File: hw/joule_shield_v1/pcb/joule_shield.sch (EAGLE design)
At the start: 136 parts, among them J1 MF-CON-MICROUSB-RIGHT, J4 USB_AUSB_A_SMT_RA, J5 JST-ZH5JST_ZH_SMT_VERT, J6 INTEL_JOULE_J6, J7 INTEL_JOULE_J7, SW1 MF-SW-TACT-4.2MM, SW2 MF-SW-TACT-4.2MM, SW3 MF-SW-TACT-4.2MM, U1 BQ25892PWQFN-24, U10 FT231XQFN-20, U11 MF-DSC-SOT233-MMBT3904, U12 MF-DSC-SOT233-MMBT3904, U13 MF-DSC-SOT233-MMBT3904, U14 MF-DSC-SOT233-MMBT3904, U2 FAN8623WLCSP16, U3 TPS63201PVSON-14, U4 TLV62084PWSON-8, U5 TPS2553PWSON-6, U6 TPS2553PWSON-6, U7 SINGLE-BIT_BUS_TRANSCEIVER, U8 SINGLE-BIT_BUS_TRANSCEIVER, U9 TXS0206-29

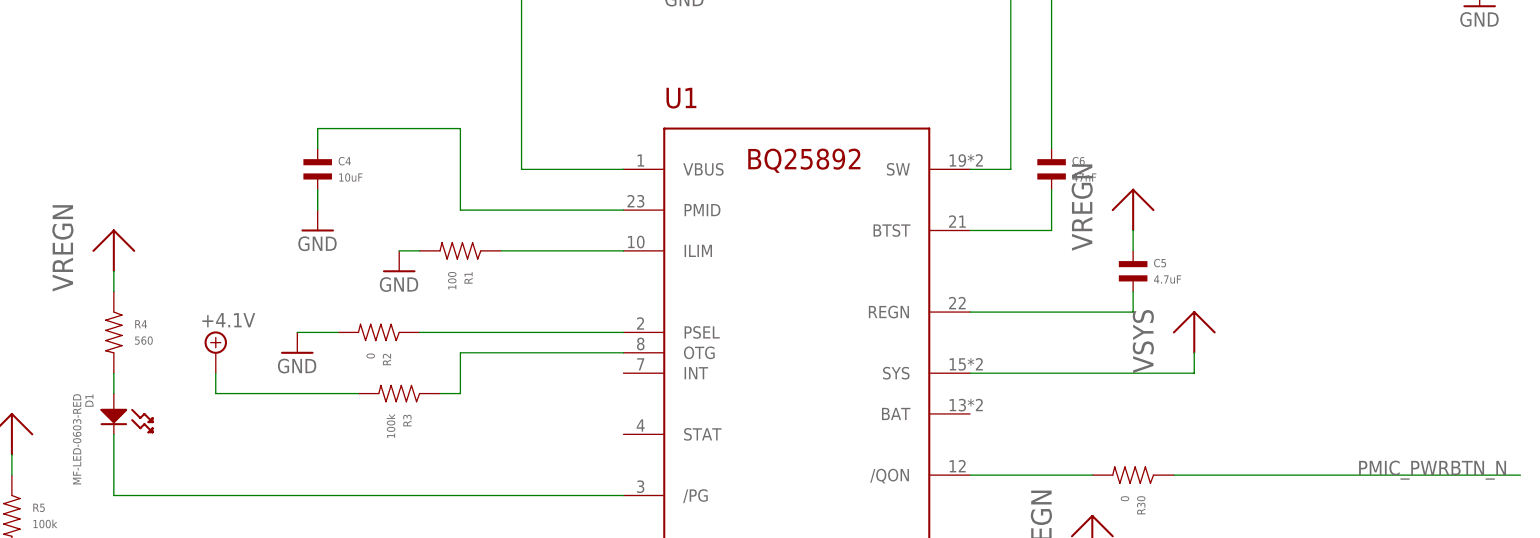
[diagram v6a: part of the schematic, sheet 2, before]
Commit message: joule shield: continue work on draft placement
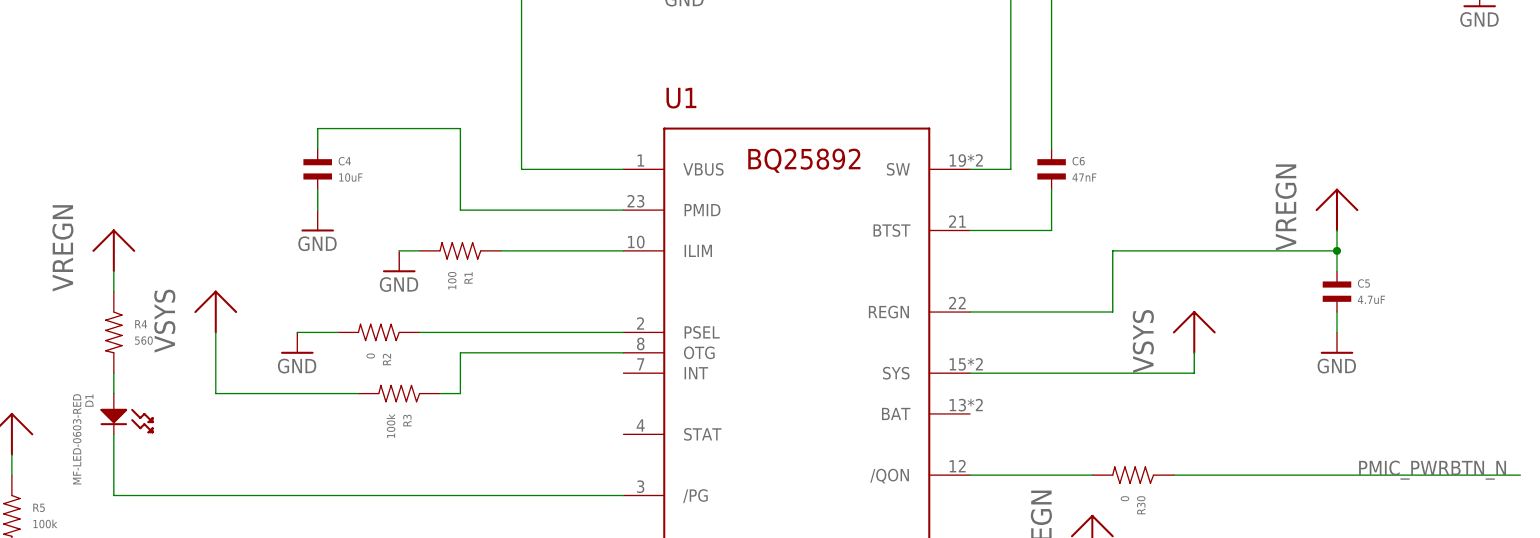
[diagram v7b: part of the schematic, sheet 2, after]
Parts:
- renumbered U$40 to J8
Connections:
- removed net +4.1V: R3.P$2
- removed net N$10: C5.P$2, U1.REGN
- net GND: now also C5.P$2
- net VREGN: now also U1.REGN
- net VSYS: now also R3.P$2
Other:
- moved on the sheet: C5
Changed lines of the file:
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@@
 <attribute name="MPN" value="MF-RES-0603-100K"/>
 </part>
-<part name="SUPPLY1" library="supply2" deviceset="+4.1V" device=""/>
 <part name="D1" library="mf_leds" deviceset="LED_SINGLE" device="-0603-RED" value="MF-LED-0603-RED"/>
 <part name="R4" library="mf_passives" deviceset="RESISTOR" device="_0603" value="560">
@@
 <part name="GND38" library="supply1" deviceset="GND" device=""/>
 <part name="GND39" library="supply1" deviceset="GND" device=""/>
-<part name="U$40" library="joule_shield" deviceset="DM3AT" device="DM3AT"/>
+<part name="J8" library="joule_shield" deviceset="DM3AT" device="DM3AT"/>
 <part name="GND40" library="supply1" deviceset="GND" device=""/>
 <part name="C36" library="mf_passives" deviceset="CAPACITOR_NP" device="_0603" value="0.1uF">
@@
 <part name="U$54" library="joule_shield" deviceset="M2.5MOUNT" device=""/>
 <part name="U$55" library="joule_shield" deviceset="M2.5MOUNT" device=""/>
+<part name="GND52" library="supply1" deviceset="GND" device=""/>
+<part name="U$40" library="joule_shield" deviceset="VSYS" device=""/>
 </parts>
 <sheets>
@@
 <instance part="GND4" gate="1" x="33.02" y="40.64"/>
 <instance part="R3" gate="G$1" x="45.72" y="35.56" rot="R270"/>
-<instance part="SUPPLY1" gate="P" x="22.86" y="40.64"/>
 <instance part="D1" gate="G$1" x="10.16" y="33.02" rot="R270"/>
 <instance part="R4" gate="G$1" x="10.16" y="43.18"/>
@@
 <instance part="R7" gate="G$1" x="132.08" y="-5.08"/>
 <instance part="GND6" gate="1" x="132.08" y="-15.24"/>
-<instance part="C5" gate="G$1" x="137.16" y="50.8">
-<attribute name="DPN" x="137.16" y="50.8" size="1.778" layer="96" display="off"/>
+<instance part="C5" gate="G$1" x="162.56" y="48.26">
+<attribute name="DPN" x="162.56" y="48.26" size="1.778" layer="96" display="off"/>
 </instance>
 <instance part="C6" gate="G$1" x="127" y="63.5">
@@
 <instance part="U$15" gate="G$1" x="180.34" y="99.06"/>
 <instance part="U$16" gate="G$1" x="144.78" y="40.64"/>
-<instance part="U$17" gate="G$1" x="137.16" y="55.88"/>
+<instance part="U$17" gate="G$1" x="162.56" y="55.88"/>
 <instance part="U$18" gate="G$1" x="132.08" y="15.24"/>
 <instance part="U$19" gate="G$1" x="10.16" y="50.8"/>
 <instance part="U$20" gate="G$1" x="60.96" y="109.22"/>
 <instance part="R30" gate="G$1" x="137.16" y="25.4" rot="R270"/>
+<instance part="GND52" gate="1" x="162.56" y="40.64"/>
+<instance part="U$40" gate="G$1" x="22.86" y="43.18"/>
 </instances>
 <busses>
@@
 <junction x="180.34" y="86.36"/>
 </segment>
+<segment>
+<pinref part="C5" gate="G$1" pin="P$2"/>
+<pinref part="GND52" gate="1" pin="GND"/>
+<wire x1="162.56" y1="45.72" x2="162.56" y2="43.18" width="0.1524" layer="91"/>
+</segment>
 </net>
 <net name="N$2" class="0">
@@
 <pinref part="U1" gate="G$1" pin="PSEL"/>
 <wire x1="48.26" y1="43.18" x2="73.66" y2="43.18" width="0.1524" layer="91"/>
-</segment>
-</net>
-<net name="+4.1V" class="0">
-<segment>
-<pinref part="SUPPLY1" gate="P" pin="+4.1V"/>
-<wire x1="22.86" y1="38.1" x2="22.86" y2="35.56" width="0.1524" layer="91"/>
-<pinref part="R3" gate="G$1" pin="P$2"/>
-<wire x1="22.86" y1="35.56" x2="40.64" y2="35.56" width="0.1524" layer="91"/>
 </segment>
 </net>
@@
 <pinref part="U1" gate="G$1" pin="TS"/>
 <wire x1="119.38" y1="10.16" x2="116.84" y2="10.16" width="0.1524" layer="91"/>
-</segment>
-</net>
-<net name="N$10" class="0">
-<segment>
-<pinref part="C5" gate="G$1" pin="P$2"/>
-<wire x1="137.16" y1="48.26" x2="137.16" y2="45.72" width="0.1524" layer="91"/>
-<pinref part="U1" gate="G$1" pin="REGN"/>
-<wire x1="137.16" y1="45.72" x2="116.84" y2="45.72" width="0.1524" layer="91"/>
 </segment>
 </net>
@@
 <pinref part="U$16" gate="G$1" pin="VSYS"/>
 </segment>
+<segment>
+<pinref part="R3" gate="G$1" pin="P$2"/>
+<wire x1="22.86" y1="35.56" x2="40.64" y2="35.56" width="0.1524" layer="91"/>
+<pinref part="U$40" gate="G$1" pin="VSYS"/>
+<wire x1="22.86" y1="35.56" x2="22.86" y2="43.18" width="0.1524" layer="91"/>
+</segment>
 </net>
 <net name="VREGN" class="0">
-<segment>
-<pinref part="C5" gate="G$1" pin="P$1"/>
-<wire x1="137.16" y1="53.34" x2="137.16" y2="55.88" width="0.1524" layer="91"/>
-<pinref part="U$17" gate="G$1" pin="VREGN"/>
-</segment>
 <segment>
 <pinref part="R6" gate="G$1" pin="P$1"/>
@@
 <wire x1="10.16" y1="50.8" x2="10.16" y2="48.26" width="0.1524" layer="91"/>
 <pinref part="U$19" gate="G$1" pin="VREGN"/>
+</segment>
+<segment>
+<pinref part="U1" gate="G$1" pin="REGN"/>
+<wire x1="116.84" y1="45.72" x2="134.62" y2="45.72" width="0.1524" layer="91"/>
+<wire x1="134.62" y1="45.72" x2="134.62" y2="53.34" width="0.1524" layer="91"/>
+<wire x1="134.62" y1="53.34" x2="162.56" y2="53.34" width="0.1524" layer="91"/>
+<pinref part="U$17" gate="G$1" pin="VREGN"/>
+<wire x1="162.56" y1="53.34" x2="162.56" y2="55.88" width="0.1524" layer="91"/>
+<pinref part="C5" gate="G$1" pin="P$1"/>
+<wire x1="162.56" y1="53.34" x2="162.56" y2="50.8" width="0.1524" layer="91"/>
+<junction x="162.56" y="53.34"/>
 </segment>
 </net>
@@
 <instance part="GND38" gate="1" x="-15.24" y="-10.16"/>
 <instance part="GND39" gate="1" x="40.64" y="22.86"/>
-<instance part="U$40" gate="G$1" x="177.8" y="22.86" rot="R180"/>
+<instance part="J8" gate="G$1" x="177.8" y="22.86" rot="R180"/>
 <instance part="GND40" gate="1" x="147.32" y="2.54"/>
 <instance part="C36" gate="G$1" x="147.32" y="58.42"/>
@@
 <pinref part="U9" gate="G$1" pin="VCCB"/>
 <wire x1="127" y1="66.04" x2="81.28" y2="66.04" width="0.1524" layer="91"/>
-<pinref part="U$40" gate="G$1" pin="VDD"/>
+<pinref part="J8" gate="G$1" pin="VDD"/>
 <wire x1="162.56" y1="30.48" x2="127" y2="30.48" width="0.1524" layer="91"/>
 <wire x1="127" y1="30.48" x2="127" y2="66.04" width="0.1524" layer="91"/>
@@
 </segment>
 <segment>
-<pinref part="U$40" gate="G$1" pin="GND"/>
+<pinref part="J8" gate="G$1" pin="GND"/>
 <wire x1="162.56" y1="33.02" x2="147.32" y2="33.02" width="0.1524" layer="91"/>
 <pinref part="GND40" gate="1" pin="GND"/>
 <wire x1="147.32" y1="33.02" x2="147.32" y2="27.94" width="0.1524" layer="91"/>
-<pinref part="U$40" gate="G$1" pin="VSS"/>
+<pinref part="J8" gate="G$1" pin="VSS"/>
 <wire x1="147.32" y1="27.94" x2="147.32" y2="5.08" width="0.1524" layer="91"/>
 <wire x1="162.56" y1="27.94" x2="147.32" y2="27.94" width="0.1524" layer="91"/>
@@
 <wire x1="147.32" y1="33.02" x2="147.32" y2="40.64" width="0.1524" layer="91"/>
 <junction x="147.32" y="33.02"/>
-<pinref part="U$40" gate="G$1" pin="CDB"/>
+<pinref part="J8" gate="G$1" pin="CDB"/>
 <wire x1="147.32" y1="40.64" x2="162.56" y2="40.64" width="0.1524" layer="91"/>
 </segment>
@@
 <net name="N$40" class="0">
 <segment>
-<pinref part="U$40" gate="G$1" pin="DAT0"/>
+<pinref part="J8" gate="G$1" pin="DAT0"/>
 <wire x1="162.56" y1="7.62" x2="121.92" y2="7.62" width="0.1524" layer="91"/>
 <wire x1="121.92" y1="7.62" x2="121.92" y2="60.96" width="0.1524" layer="91"/>
@@
 <net name="N$41" class="0">
 <segment>
-<pinref part="U$40" gate="G$1" pin="DAT1"/>
+<pinref part="J8" gate="G$1" pin="DAT1"/>
 <wire x1="162.56" y1="10.16" x2="119.38" y2="10.16" width="0.1524" layer="91"/>
 <wire x1="119.38" y1="10.16" x2="119.38" y2="58.42" width="0.1524" layer="91"/>
@@
 <net name="N$42" class="0">
 <segment>
-<pinref part="U$40" gate="G$1" pin="DAT2"/>
+<pinref part="J8" gate="G$1" pin="DAT2"/>
 <wire x1="162.56" y1="12.7" x2="116.84" y2="12.7" width="0.1524" layer="91"/>
 <wire x1="116.84" y1="12.7" x2="116.84" y2="55.88" width="0.1524" layer="91"/>
@@
 <net name="N$43" class="0">
 <segment>
-<pinref part="U$40" gate="G$1" pin="CD/DAT3"/>
+<pinref part="J8" gate="G$1" pin="CD/DAT3"/>
 <wire x1="162.56" y1="15.24" x2="114.3" y2="15.24" width="0.1524" layer="91"/>
 <wire x1="114.3" y1="15.24" x2="114.3" y2="53.34" width="0.1524" layer="91"/>
@@
 <net name="N$44" class="0">
 <segment>
-<pinref part="U$40" gate="G$1" pin="CMD"/>
+<pinref part="J8" gate="G$1" pin="CMD"/>
 <wire x1="162.56" y1="22.86" x2="111.76" y2="22.86" width="0.1524" layer="91"/>
 <wire x1="111.76" y1="22.86" x2="111.76" y2="48.26" width="0.1524" layer="91"/>
@@
 <net name="N$45" class="0">
 <segment>
-<pinref part="U$40" gate="G$1" pin="CLK"/>
+<pinref part="J8" gate="G$1" pin="CLK"/>
 <wire x1="162.56" y1="20.32" x2="109.22" y2="20.32" width="0.1524" layer="91"/>
 <wire x1="109.22" y1="20.32" x2="109.22" y2="45.72" width="0.1524" layer="91"/>
@@
 <segment>
 <pinref part="U9" gate="G$1" pin="WP/CD"/>
-<pinref part="U$40" gate="G$1" pin="CDA"/>
+<pinref part="J8" gate="G$1" pin="CDA"/>
 <wire x1="81.28" y1="38.1" x2="162.56" y2="38.1" width="0.1524" layer="91"/>
 <label x="86.36" y="38.1" size="1.778" layer="95"/>

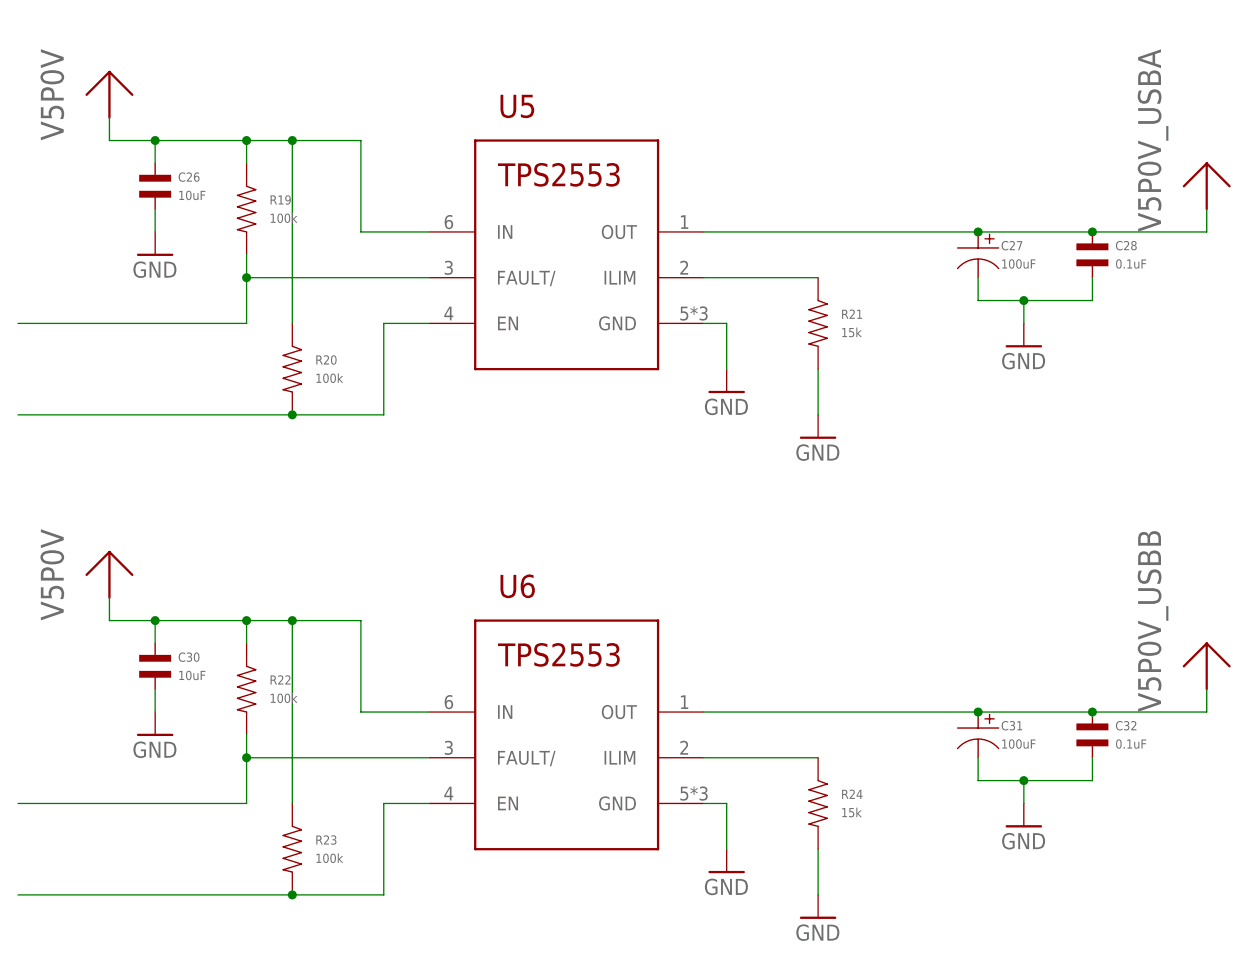
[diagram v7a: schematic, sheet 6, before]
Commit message: Replace USB electrolytics with ceramics.  Get everything placed but the RTC battery.
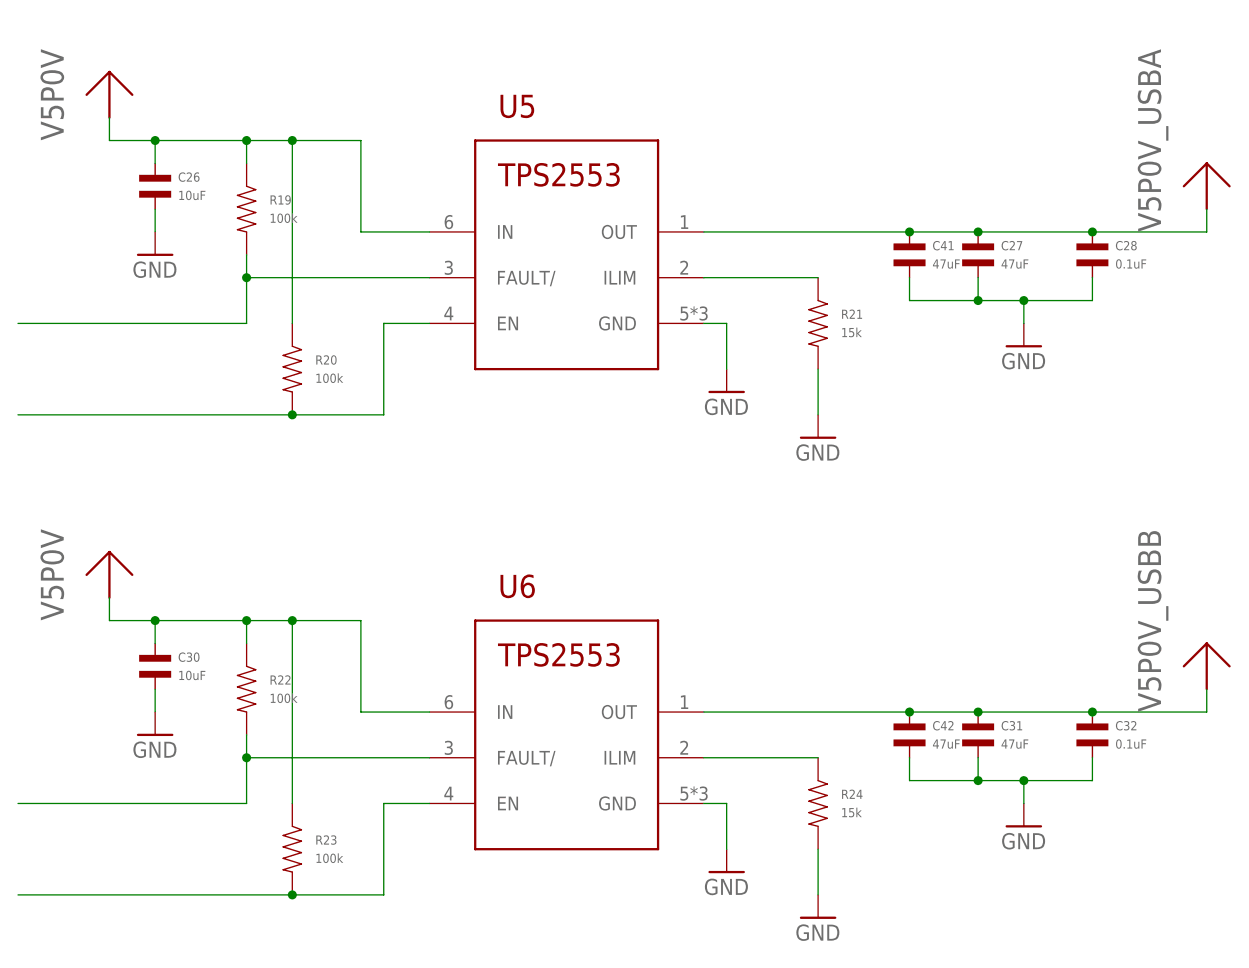
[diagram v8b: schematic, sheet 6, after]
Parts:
- added C41, C42: 47uF, mf_passives:CAPACITOR_NP_0805
- C27, C31: value 100uF -> 47uF; device mf_passives:CAPACITOR_P_6.3MM -> mf_passives:CAPACITOR_NP_0805; DPN (none) -> 445-8239-1-ND; MPN MF-CAP-6.3MM-100uF -> C2012X5R1A476M125AC
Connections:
- net GND: now also C41.P$2, C42.P$2
- net V5P0V_USBA: now also C41.P$1
- net V5P0V_USBB: now also C42.P$1
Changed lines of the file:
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@@
 </part>
 <part name="GND22" library="supply1" deviceset="GND" device=""/>
-<part name="C27" library="mf_passives" deviceset="CAPACITOR_P" device="_6.3MM" value="100uF">
-<attribute name="MPN" value="MF-CAP-6.3MM-100uF"/>
+<part name="C27" library="mf_passives" deviceset="CAPACITOR_NP" device="_0805" value="47uF">
+<attribute name="DPN" value="445-8239-1-ND"/>
+<attribute name="MPN" value="C2012X5R1A476M125AC"/>
 </part>
 <part name="C28" library="mf_passives" deviceset="CAPACITOR_NP" device="_0603" value="0.1uF">
@@
 </part>
 <part name="GND32" library="supply1" deviceset="GND" device=""/>
-<part name="C31" library="mf_passives" deviceset="CAPACITOR_P" device="_6.3MM" value="100uF">
-<attribute name="MPN" value="MF-CAP-6.3MM-100uF"/>
+<part name="C31" library="mf_passives" deviceset="CAPACITOR_NP" device="_0805" value="47uF">
+<attribute name="DPN" value="445-8239-1-ND"/>
+<attribute name="MPN" value="C2012X5R1A476M125AC"/>
 </part>
 <part name="C32" library="mf_passives" deviceset="CAPACITOR_NP" device="_0603" value="0.1uF">
@@
 <part name="GND52" library="supply1" deviceset="GND" device=""/>
 <part name="U$40" library="joule_shield" deviceset="VSYS" device=""/>
+<part name="C41" library="mf_passives" deviceset="CAPACITOR_NP" device="_0805" value="47uF">
+<attribute name="DPN" value="445-8239-1-ND"/>
+<attribute name="MPN" value="C2012X5R1A476M125AC"/>
+</part>
+<part name="C42" library="mf_passives" deviceset="CAPACITOR_NP" device="_0805" value="47uF">
+<attribute name="DPN" value="445-8239-1-ND"/>
+<attribute name="MPN" value="C2012X5R1A476M125AC"/>
+</part>
 </parts>
 <sheets>
@@
 <instance part="R21" gate="G$1" x="106.68" y="45.72"/>
 <instance part="GND22" gate="1" x="106.68" y="33.02"/>
-<instance part="C27" gate="G$1" x="124.46" y="53.34"/>
+<instance part="C27" gate="G$1" x="124.46" y="53.34">
+<attribute name="DPN" x="124.46" y="53.34" size="1.778" layer="96" display="off"/>
+</instance>
 <instance part="C28" gate="G$1" x="137.16" y="53.34"/>
 <instance part="GND23" gate="1" x="129.54" y="43.18"/>
@@
 <instance part="R24" gate="G$1" x="106.68" y="-7.62"/>
 <instance part="GND32" gate="1" x="106.68" y="-20.32"/>
-<instance part="C31" gate="G$1" x="124.46" y="0"/>
+<instance part="C31" gate="G$1" x="124.46" y="0">
+<attribute name="DPN" x="124.46" y="0" size="1.778" layer="96" display="off"/>
+</instance>
 <instance part="C32" gate="G$1" x="137.16" y="0"/>
 <instance part="GND33" gate="1" x="129.54" y="-10.16"/>
 <instance part="U$35" gate="G$1" x="149.86" y="5.08"/>
+<instance part="C41" gate="G$1" x="116.84" y="53.34">
+<attribute name="DPN" x="116.84" y="53.34" size="1.778" layer="96" display="off"/>
+</instance>
+<instance part="C42" gate="G$1" x="116.84" y="0">
+<attribute name="DPN" x="116.84" y="0" size="1.778" layer="96" display="off"/>
+</instance>
 </instances>
 <busses>
@@
 <wire x1="137.16" y1="48.26" x2="137.16" y2="50.8" width="0.1524" layer="91"/>
 <junction x="129.54" y="48.26"/>
+<pinref part="C41" gate="G$1" pin="P$2"/>
+<wire x1="116.84" y1="50.8" x2="116.84" y2="48.26" width="0.1524" layer="91"/>
+<wire x1="116.84" y1="48.26" x2="124.46" y2="48.26" width="0.1524" layer="91"/>
+<junction x="124.46" y="48.26"/>
 </segment>
 <segment>
@@
 <wire x1="137.16" y1="-5.08" x2="137.16" y2="-2.54" width="0.1524" layer="91"/>
 <junction x="129.54" y="-5.08"/>
+<pinref part="C42" gate="G$1" pin="P$2"/>
+<wire x1="116.84" y1="-2.54" x2="116.84" y2="-5.08" width="0.1524" layer="91"/>
+<wire x1="116.84" y1="-5.08" x2="124.46" y2="-5.08" width="0.1524" layer="91"/>
+<junction x="124.46" y="-5.08"/>
 </segment>
 </net>
@@
 <pinref part="U5" gate="G$1" pin="OUT"/>
 <pinref part="C27" gate="G$1" pin="P$1"/>
-<wire x1="93.98" y1="55.88" x2="124.46" y2="55.88" width="0.1524" layer="91"/>
+<wire x1="93.98" y1="55.88" x2="116.84" y2="55.88" width="0.1524" layer="91"/>
 <pinref part="C28" gate="G$1" pin="P$1"/>
+<wire x1="116.84" y1="55.88" x2="124.46" y2="55.88" width="0.1524" layer="91"/>
 <wire x1="124.46" y1="55.88" x2="137.16" y2="55.88" width="0.1524" layer="91"/>
 <junction x="124.46" y="55.88"/>
@@
 <wire x1="149.86" y1="55.88" x2="149.86" y2="58.42" width="0.1524" layer="91"/>
 <junction x="137.16" y="55.88"/>
+<pinref part="C41" gate="G$1" pin="P$1"/>
+<junction x="116.84" y="55.88"/>
 </segment>
 </net>
@@
 <pinref part="U6" gate="G$1" pin="OUT"/>
 <pinref part="C31" gate="G$1" pin="P$1"/>
-<wire x1="93.98" y1="2.54" x2="124.46" y2="2.54" width="0.1524" layer="91"/>
+<wire x1="93.98" y1="2.54" x2="116.84" y2="2.54" width="0.1524" layer="91"/>
 <pinref part="C32" gate="G$1" pin="P$1"/>
+<wire x1="116.84" y1="2.54" x2="124.46" y2="2.54" width="0.1524" layer="91"/>
 <wire x1="124.46" y1="2.54" x2="137.16" y2="2.54" width="0.1524" layer="91"/>
 <junction x="124.46" y="2.54"/>
@@
 <junction x="137.16" y="2.54"/>
 <pinref part="U$35" gate="G$1" pin="V5P0V_USBB"/>
-</segment>
-</net>
+<pinref part="C42" gate="G$1" pin="P$1"/>
+<junction x="116.84" y="2.54"/>
+</segment>
+</net>
